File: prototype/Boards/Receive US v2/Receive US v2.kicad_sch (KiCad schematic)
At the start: 47 parts, among them J1 Conn_01x04_Socket, Q1 MMBT3904, Q3 MMBT3904, U1 LM324

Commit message: Recv V2 layout
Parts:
- R19: now not fitted
- TP1, TP2: footprint TestPoint:TestPoint_THTPad_D1.5mm_Drill0.7mm -> uFinder:TestPoint_THTPad_D1.5mm_Drill0.7mm; symbol Connector:TestPoint -> uFinder:TestPoint; Label (none) -> GND
- TP3: footprint TestPoint:TestPoint_THTPad_D1.5mm_Drill0.7mm -> uFinder:TestPoint_THTPad_D1.5mm_Drill0.7mm; symbol Connector:TestPoint -> uFinder:TestPoint; Label (none) -> Stg 2 In; Net (none) -> Foo
- TP4: footprint TestPoint:TestPoint_THTPad_D1.5mm_Drill0.7mm -> uFinder:TestPoint_THTPad_D1.5mm_Drill0.7mm; symbol Connector:TestPoint -> uFinder:TestPoint; Label (none) -> REF
- TP5: footprint TestPoint:TestPoint_THTPad_D1.5mm_Drill0.7mm -> uFinder:TestPoint_THTPad_D1.5mm_Drill0.7mm; symbol Connector:TestPoint -> uFinder:TestPoint; Label (none) -> Stg 3 In
- TP6: footprint TestPoint:TestPoint_THTPad_D1.5mm_Drill0.7mm -> uFinder:TestPoint_THTPad_D1.5mm_Drill0.7mm; symbol Connector:TestPoint -> uFinder:TestPoint; Label (none) -> Stg 4 In; Net (none) -> Foo
- TP7: footprint TestPoint:TestPoint_THTPad_D1.5mm_Drill0.7mm -> uFinder:TestPoint_THTPad_D1.5mm_Drill0.7mm; symbol Connector:TestPoint -> uFinder:TestPoint; Label (none) -> Stg 4 Out; Net (none) -> Foo
- TP8: footprint TestPoint:TestPoint_THTPad_D1.5mm_Drill0.7mm -> uFinder:TestPoint_THTPad_D1.5mm_Drill0.7mm; symbol Connector:TestPoint -> uFinder:TestPoint; Label (none) -> Data
- renumbered Q3 to Q2
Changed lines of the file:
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@@
     )
   )
-  (symbol (lib_id "Connector:TestPoint") (at 50.8 128.27 0) (unit 1)
-    (in_bom yes) (on_board yes) (dnp no) (fields_autoplaced)
+  (symbol (lib_name "TestPoint_1") (lib_id "uFinder:TestPoint") (at 50.8 128.27 0) (unit 1)
+    (in_bom yes) (on_board yes) (dnp no)
     (property "Reference" "TP1" (at 53.34 124.333 0)
       (effects (font (size 1.27 1.27)) (justify left))
@@
       (effects (font (size 1.27 1.27)) (justify left))
     )
-    (property "Footprint" "TestPoint:TestPoint_THTPad_D1.5mm_Drill0.7mm" (at 55.88 128.27 0)
+    (property "Footprint" "uFinder:TestPoint_THTPad_D1.5mm_Drill0.7mm" (at 55.88 128.27 0)
       (effects (font (size 1.27 1.27)) hide)
     )
     (property "Datasheet" "~" (at 55.88 128.27 0)
       (effects (font (size 1.27 1.27)) hide)
+    )
+    (property "Label" "GND" (at 55.88 129.54 0)
+      (effects (font (size 1.27 1.27)))
     )
     (pin "1")
@@
     )
   )
-  (symbol (lib_id "Connector:TestPoint") (at 116.84 86.36 0) (unit 1)
+  (symbol (lib_name "TestPoint_3") (lib_id "uFinder:TestPoint") (at 116.84 86.36 0) (unit 1)
     (in_bom yes) (on_board yes) (dnp no)
     (property "Reference" "TP4" (at 119.38 82.423 0)
@@
       (effects (font (size 1.27 1.27)) (justify left))
     )
-    (property "Footprint" "TestPoint:TestPoint_THTPad_D1.5mm_Drill0.7mm" (at 121.92 86.36 0)
+    (property "Footprint" "uFinder:TestPoint_THTPad_D1.5mm_Drill0.7mm" (at 121.92 86.36 0)
       (effects (font (size 1.27 1.27)) hide)
     )
@@
       (effects (font (size 1.27 1.27)) hide)
     )
+    (property "Label" "REF" (at 121.285 86.995 0)
+      (effects (font (size 1.27 1.27)))
+    )
     (pin "1")
     (instances
@@
     )
   )
-  (symbol (lib_id "Connector:TestPoint") (at 156.21 41.91 0) (mirror y) (unit 1)
+  (symbol (lib_id "uFinder:TestPoint") (at 156.21 41.91 0) (mirror y) (unit 1)
     (in_bom yes) (on_board yes) (dnp no)
     (property "Reference" "TP5" (at 153.67 37.973 0)
@@
       (effects (font (size 1.27 1.27)) (justify left))
     )
-    (property "Footprint" "TestPoint:TestPoint_THTPad_D1.5mm_Drill0.7mm" (at 151.13 41.91 0)
+    (property "Footprint" "uFinder:TestPoint_THTPad_D1.5mm_Drill0.7mm" (at 151.13 41.91 0)
       (effects (font (size 1.27 1.27)) hide)
     )
@@
       (effects (font (size 1.27 1.27)) hide)
     )
+    (property "Net" "" (at 156.21 36.83 0)
+      (effects (font (size 0.8 0.8)))
+    )
+    (property "Label" "Stg 3 In" (at 151.13 43.18 0)
+      (effects (font (size 1.27 1.27)))
+    )
     (pin "1")
     (instances
@@
     )
   )
-  (symbol (lib_id "Connector:TestPoint") (at 190.5 41.91 0) (mirror y) (unit 1)
+  (symbol (lib_id "uFinder:TestPoint") (at 190.5 41.91 0) (mirror y) (unit 1)
     (in_bom yes) (on_board yes) (dnp no)
     (property "Reference" "TP6" (at 187.96 37.973 0)
@@
       (effects (font (size 1.27 1.27)) (justify left))
     )
-    (property "Footprint" "TestPoint:TestPoint_THTPad_D1.5mm_Drill0.7mm" (at 185.42 41.91 0)
+    (property "Footprint" "uFinder:TestPoint_THTPad_D1.5mm_Drill0.7mm" (at 185.42 41.91 0)
       (effects (font (size 1.27 1.27)) hide)
     )
     (property "Datasheet" "~" (at 185.42 41.91 0)
       (effects (font (size 1.27 1.27)) hide)
+    )
+    (property "Net" "Foo" (at 190.5 36.83 0)
+      (effects (font (size 0.8 0.8)))
+    )
+    (property "Label" "Stg 4 In" (at 185.42 43.18 0)
+      (effects (font (size 1.27 1.27)))
     )
     (pin "1")
@@
   )
   (symbol (lib_id "Device:R") (at 30.48 58.42 180) (unit 1)
-    (in_bom yes) (on_board yes) (dnp no) (fields_autoplaced)
+    (in_bom yes) (on_board yes) (dnp yes) (fields_autoplaced)
     (property "Reference" "R19" (at 33.02 57.785 0)
       (effects (font (size 1.27 1.27)) (justify right))
@@
     )
   )
-  (symbol (lib_id "Connector:TestPoint") (at 63.5 128.27 0) (unit 1)
-    (in_bom yes) (on_board yes) (dnp no) (fields_autoplaced)
+  (symbol (lib_name "TestPoint_2") (lib_id "uFinder:TestPoint") (at 63.5 128.27 0) (unit 1)
+    (in_bom yes) (on_board yes) (dnp no)
     (property "Reference" "TP2" (at 66.04 124.333 0)
       (effects (font (size 1.27 1.27)) (justify left))
@@
       (effects (font (size 1.27 1.27)) (justify left))
     )
-    (property "Footprint" "TestPoint:TestPoint_THTPad_D1.5mm_Drill0.7mm" (at 68.58 128.27 0)
+    (property "Footprint" "uFinder:TestPoint_THTPad_D1.5mm_Drill0.7mm" (at 68.58 128.27 0)
       (effects (font (size 1.27 1.27)) hide)
     )
     (property "Datasheet" "~" (at 68.58 128.27 0)
       (effects (font (size 1.27 1.27)) hide)
+    )
+    (property "Label" "GND" (at 68.58 129.54 0)
+      (effects (font (size 1.27 1.27)))
     )
     (pin "1")
@@
     )
   )
-  (symbol (lib_id "Connector:TestPoint") (at 104.14 35.56 0) (mirror y) (unit 1)
+  (symbol (lib_id "uFinder:TestPoint") (at 104.14 35.56 0) (mirror y) (unit 1)
     (in_bom yes) (on_board yes) (dnp no)
     (property "Reference" "TP3" (at 101.6 31.623 0)
@@
       (effects (font (size 1.27 1.27)) (justify left))
     )
-    (property "Footprint" "TestPoint:TestPoint_THTPad_D1.5mm_Drill0.7mm" (at 99.06 35.56 0)
+    (property "Footprint" "uFinder:TestPoint_THTPad_D1.5mm_Drill0.7mm" (at 99.06 35.56 0)
       (effects (font (size 1.27 1.27)) hide)
     )
     (property "Datasheet" "~" (at 99.06 35.56 0)
       (effects (font (size 1.27 1.27)) hide)
+    )
+    (property "Net" "Foo" (at 104.14 30.48 0)
+      (effects (font (size 0.8 0.8)))
+    )
+    (property "Label" "Stg 2 In" (at 97.79 36.83 0)
+      (effects (font (size 1.27 1.27)))
     )
     (pin "1")
@@
     )
   )
-  (symbol (lib_id "Connector:TestPoint") (at 262.89 41.91 0) (mirror y) (unit 1)
+  (symbol (lib_id "uFinder:TestPoint") (at 262.89 41.91 0) (mirror y) (unit 1)
     (in_bom yes) (on_board yes) (dnp no)
     (property "Reference" "TP8" (at 260.35 37.973 0)
@@
       (effects (font (size 1.27 1.27)) (justify left))
     )
-    (property "Footprint" "TestPoint:TestPoint_THTPad_D1.5mm_Drill0.7mm" (at 257.81 41.91 0)
+    (property "Footprint" "uFinder:TestPoint_THTPad_D1.5mm_Drill0.7mm" (at 257.81 41.91 0)
       (effects (font (size 1.27 1.27)) hide)
     )
     (property "Datasheet" "~" (at 257.81 41.91 0)
       (effects (font (size 1.27 1.27)) hide)
+    )
+    (property "Label" "Data" (at 257.81 43.18 0)
+      (effects (font (size 1.27 1.27)))
     )
     (pin "1")
@@
   (symbol (lib_id "Transistor_BJT:MMBT3904") (at 242.57 55.88 0) (unit 1)
     (in_bom yes) (on_board yes) (dnp no) (fields_autoplaced)
-    (property "Reference" "Q3" (at 247.65 55.245 0)
+    (property "Reference" "Q2" (at 247.65 55.245 0)
       (effects (font (size 1.27 1.27)) (justify left))
     )
@@
       (project "Receive US v2"
         (path "/0eda4ce1-66e5-46e6-bd69-aabda35926fc"
-          (reference "Q3") (unit 1)
+          (reference "Q2") (unit 1)
         )
       )
@@
     )
   )
-  (symbol (lib_id "Connector:TestPoint") (at 218.44 52.07 0) (mirror y) (unit 1)
+  (symbol (lib_id "uFinder:TestPoint") (at 218.44 52.07 0) (mirror y) (unit 1)
     (in_bom yes) (on_board yes) (dnp no)
     (property "Reference" "TP7" (at 215.9 48.133 0)
@@
       (effects (font (size 1.27 1.27)) (justify left))
     )
-    (property "Footprint" "TestPoint:TestPoint_THTPad_D1.5mm_Drill0.7mm" (at 213.36 52.07 0)
+    (property "Footprint" "uFinder:TestPoint_THTPad_D1.5mm_Drill0.7mm" (at 213.36 52.07 0)
       (effects (font (size 1.27 1.27)) hide)
     )
@@
       (effects (font (size 1.27 1.27)) hide)
     )
-    (pin "1")
+    (property "Net" "Foo" (at 218.44 46.99 0)
+      (effects (font (size 0.8 0.8)))
+    )
+    (property "Label" "Stg 4 Out" (at 224.79 48.26 0)
+      (effects (font (size 1.27 1.27)))
+    )
+    (pin "1")

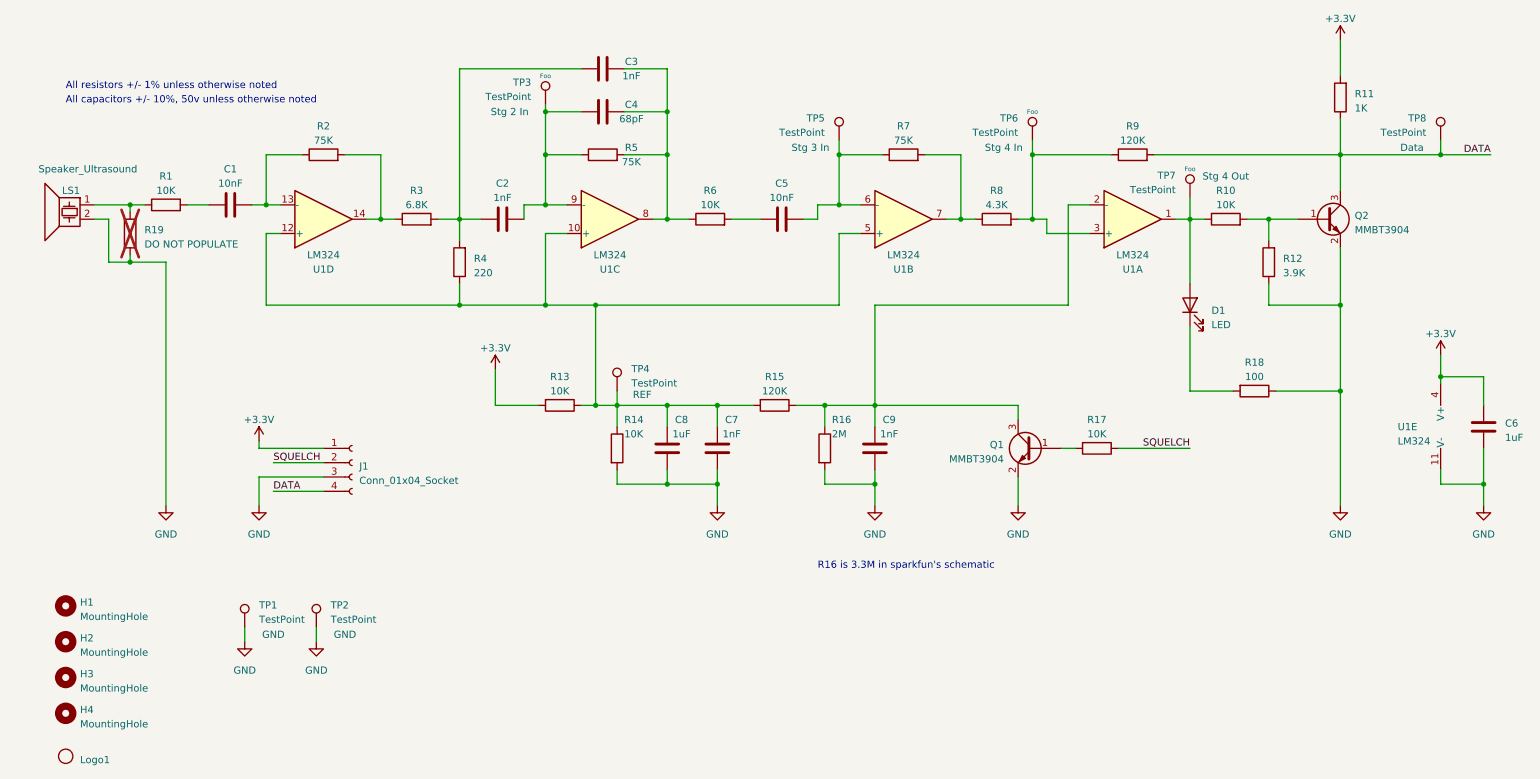
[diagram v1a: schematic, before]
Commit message: Second try for receive PCB layout
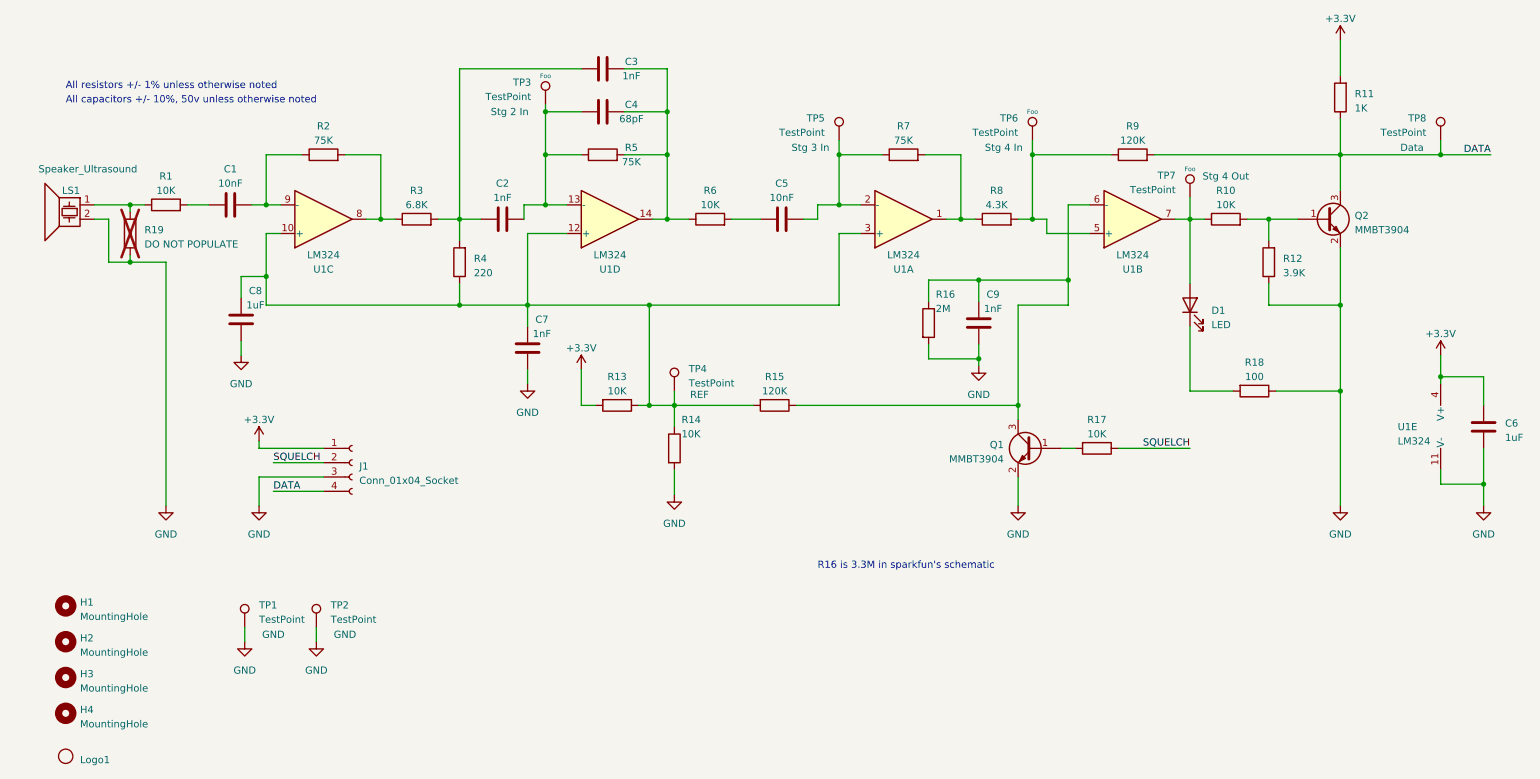
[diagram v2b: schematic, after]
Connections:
- net at C9.2, Q1.3 (C), R15.1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: now also U1.6 (-); no longer U1.2 (-)
- net at C1.2, R2.1: now also U1.9 (-); no longer U1.13 (-)
- net at R8.2, R9.1, TP6.1: now also U1.5 (+); no longer U1.3 (+)
- net at C7.2, C8.2, R13.1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: now also U1.3 (+); no longer U1.5 (+)
- net at C5.2, R7.1, TP5.1: now also U1.2 (-); no longer U1.6 (-)
- net at R7.2, R8.1: now also U1.1; no longer U1.7
- net at C2.2, C4.1, R5.1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: now also U1.13 (-); no longer U1.9 (-)
- net at C3.2, C4.2, R5.2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: now also U1.14; no longer U1.8
- net at D1.2 (A), R10.1, TP7.1: now also U1.7; no longer U1.1
- net at R2.2, R3.1: now also U1.8; no longer U1.14
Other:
- moved on the sheet: C7, C8, C9, R13, R14, R16, TP4, U1A, U1B, U1C, U1D
